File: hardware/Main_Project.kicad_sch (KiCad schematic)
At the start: 53 parts, among them J1 A_Motor, J2 B_Motor, J3 Power_Outputs, U1 L7805, U2 L298N, U4 L298N

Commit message: Motor Board
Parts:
- removed C6, C8, C9: 4.7uF, Capacitor_THT:CP_Radial_D10.0mm_P5.00mm, symbol Device:C_Polarized_US
- removed C7: 100nF, Capacitor_THT:C_Disc_D8.0mm_W2.5mm_P5.00mm, symbol Device:C
- removed D13, D14, D15, D16, D17, D18, D19, D20: D, Diode_THT:D_A-405_P10.16mm_Horizontal, symbol Device:D
- removed J1: A_Motor, TerminalBlock:TerminalBlock_bornier-2_P5.08mm, symbol Connector:Conn_01x04_Pin
- removed J2: B_Motor, TerminalBlock:TerminalBlock_bornier-2_P5.08mm, symbol Connector:Conn_01x04_Pin
- removed R10, R5, R6, R9: 1k, Resistor_THT:R_Axial_DIN0207_L6.3mm_D2.5mm_P10.16mm_Horizontal, symbol Device:R
- removed R3, R4, R7, R8: 10k, Resistor_THT:R_Axial_DIN0207_L6.3mm_D2.5mm_P10.16mm_Horizontal, symbol Device:R
- removed U4: L298N, Package_TO_SOT_THT:TO-220-15_P2.54x2.54mm_StaggerOdd_Lead4.58mm_Vertical, symbol Driver_Motor:L298N
- added H10, H9: HeatsinkMounting, new_winterbloom:M3_Heatsink_Mounting, symbol Mechanical:MountingHole
- added H5, H6, H7, H8: MountingHole, MountingHole:MountingHole_3mm, symbol Mechanical:MountingHole
- added J1: Motors_R, TerminalBlock:TerminalBlock_bornier-2_P5.08mm, symbol Connector:Conn_01x02_Socket
- added J2: Motors_L, TerminalBlock:TerminalBlock_bornier-2_P5.08mm, symbol Connector:Conn_01x02_Socket
- added J4: Motor_Control, Connector_Molex:Molex_KK-396_5273-06A_1x06_P3.96mm_Vertical, symbol Connector:Conn_01x06_Pin
- added J5: Motor_Power, TerminalBlock:TerminalBlock_bornier-3_P5.08mm, symbol Connector:Conn_01x03_Pin
- C5: footprint Capacitor_THT:CP_Radial_D10.0mm_P5.00mm -> Capacitor_THT:CP_Radial_D8.0mm_P3.50mm
- U1: footprint Package_TO_SOT_THT:TO-220-3_Vertical -> Package_TO_SOT_THT:TO-220-3_Horizontal_TabDown
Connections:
- net +12V: now also J5.1 (Pin_1)
- net +5V: now also J5.2 (Pin_2)
- net GND: now also U2.1 (SENSE_A), U2.15 (SENSE_B), J5.3 (Pin_3)
- net at D5.2 (A), D9.1 (K), U2.2 (OUT1): now also J2.1 (Pin_1)
- net at D10.1 (K), D6.2 (A), U2.3 (OUT2): now also J2.2 (Pin_2)
- net R_Enable: now reaches U2.11 (EnB)
- net R_Enable: now also J4.3 (Pin_3)
- net at D11.1 (K), D7.2 (A), U2.13 (OUT3): now also J1.1 (Pin_1)
- net at D12.1 (K), D8.2 (A), U2.14 (OUT4): now also J1.2 (Pin_2)
- net L_Enable: now reaches U2.6 (EnA)
- net L_Enable: now also J4.6 (Pin_6)
- net A_Motor1 renamed L_1
- net L_1: now also J4.1 (Pin_1)
- net A_Motor2 renamed L_2
- net L_2: now also J4.2 (Pin_2)
- net A_Motor3 renamed R_1
- net R_1: now also J4.5 (Pin_5)
- net A_Motor4 renamed R_2
- net R_2: now also J4.4 (Pin_4)
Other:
- note added: "Motor Driver"
- note removed: "Motor Driver A"
- note removed: "Motor Driver B"

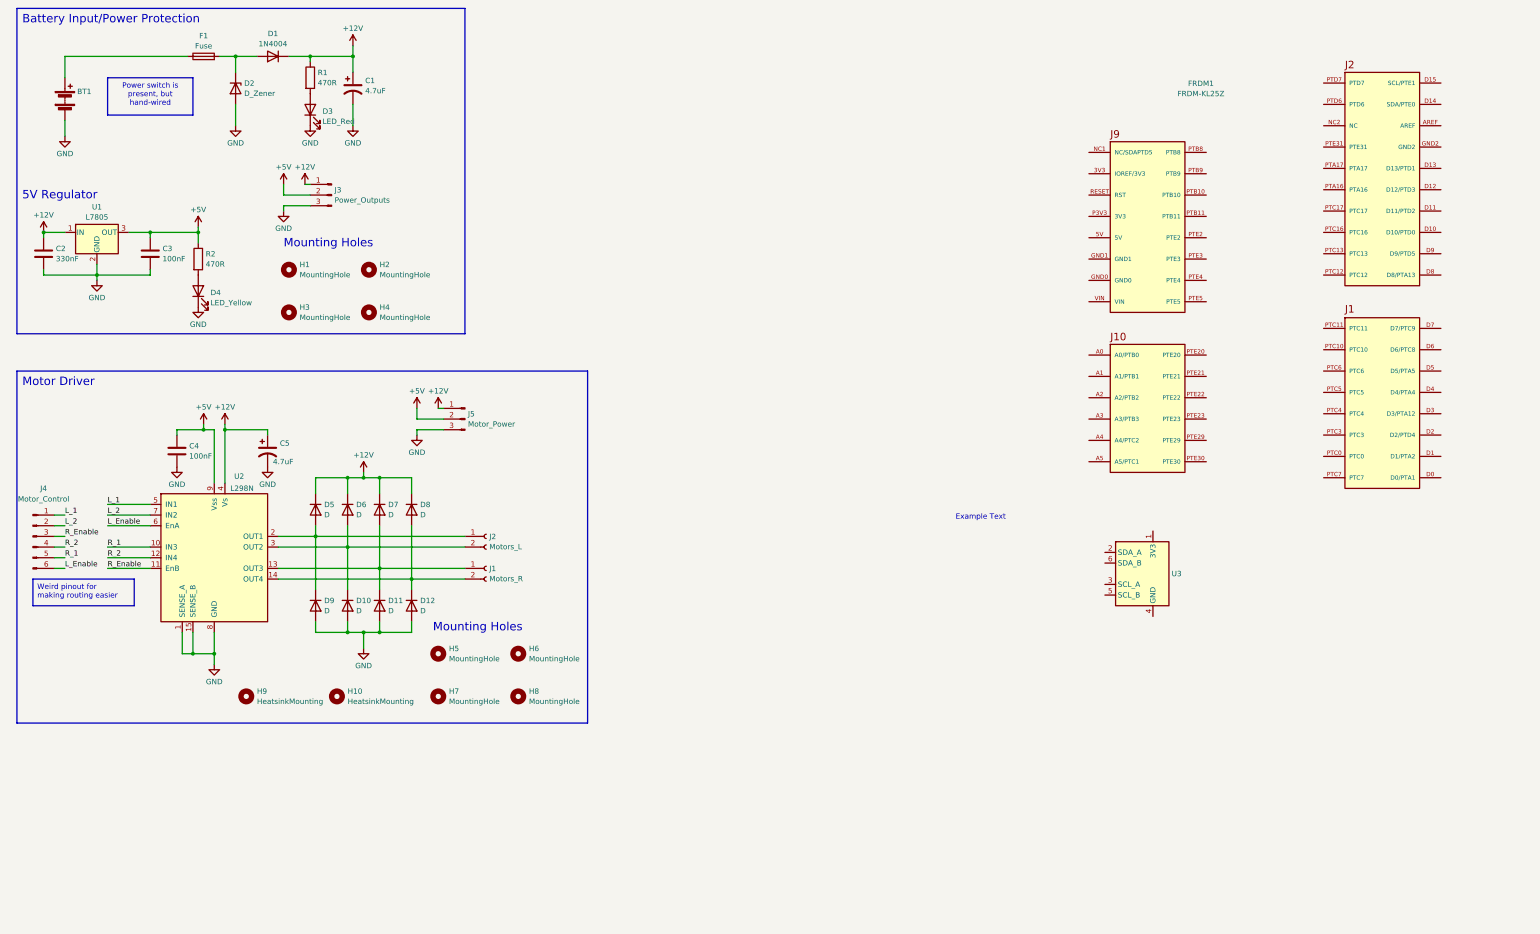
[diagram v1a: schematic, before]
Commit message: Colour Sensor board added and adjusted
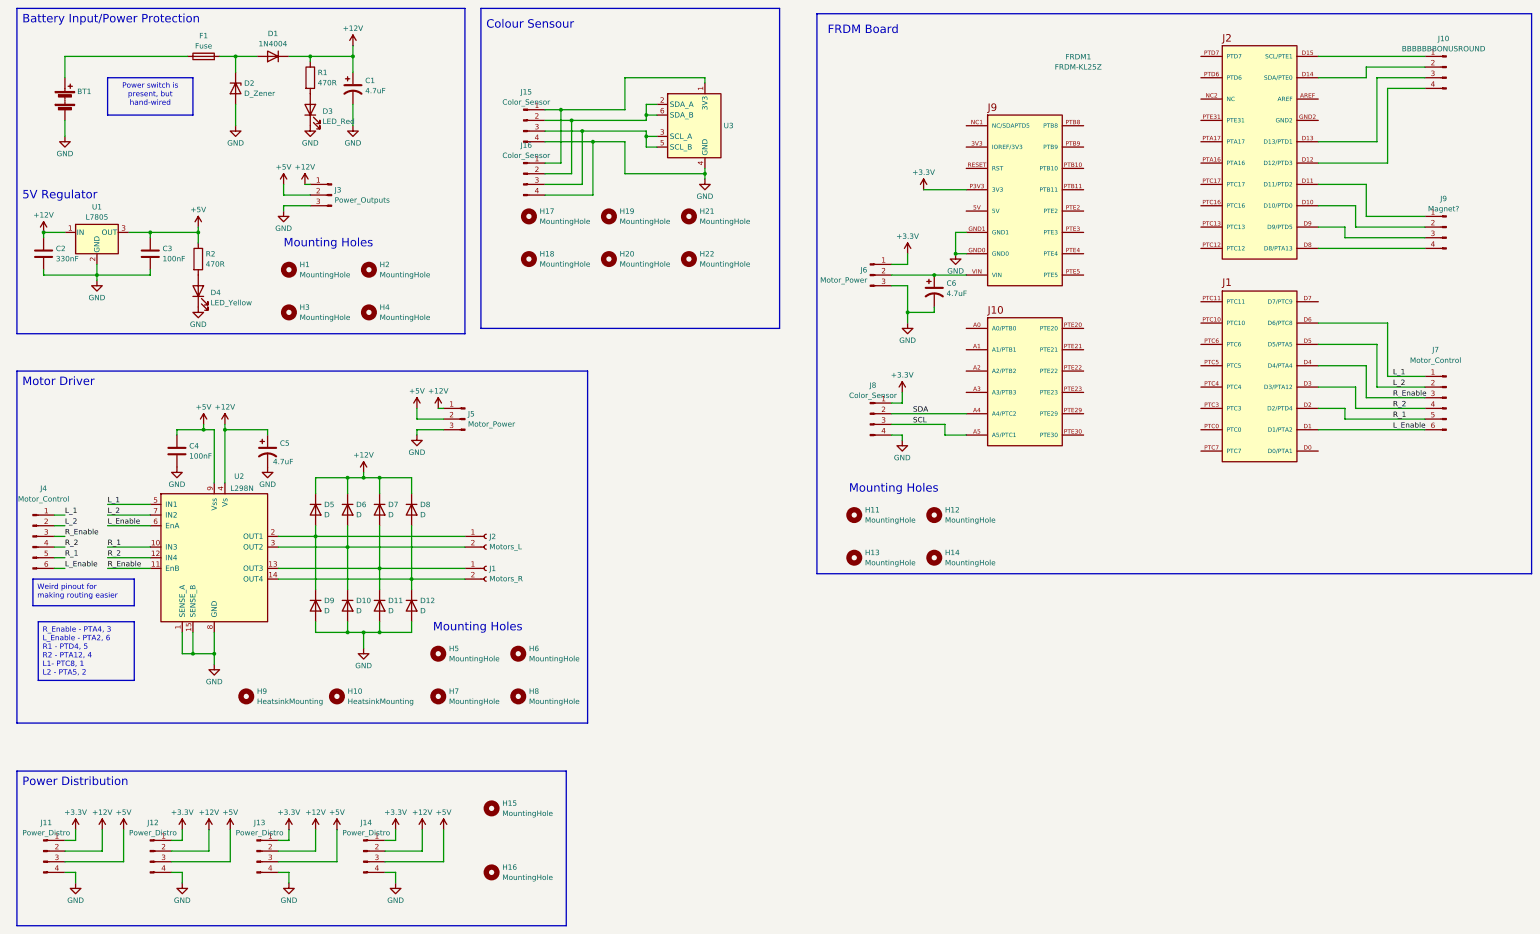
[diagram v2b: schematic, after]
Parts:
- added C6: 4.7uF, Capacitor_THT:CP_Radial_D8.0mm_P3.50mm, symbol Device:C_Polarized_US
- added H11, H12, H13, H14, H15, H16, H17, H18, H19, H20: MountingHole, MountingHole:MountingHole_3mm, symbol Mechanical:MountingHole
- added H21, H22: MountingHole, MountingHole:MountingHole_5.3mm_M5, symbol Mechanical:MountingHole
- added J10: BBBBBBBONUSROUND, Connector_Molex:Molex_KK-254_AE-6410-04A_1x04_P2.54mm_Vertical, symbol Connector:Conn_01x04_Pin
- added J11, J12, J13, J14: Power_Distro, TerminalBlock:TerminalBlock_bornier-4_P5.08mm, symbol Connector:Conn_01x04_Pin
- added J15, J16, J8: Color_Sensor, Connector_Molex:Molex_KK-254_AE-6410-04A_1x04_P2.54mm_Vertical, symbol Connector:Conn_01x04_Pin
- added J6: Motor_Power, TerminalBlock:TerminalBlock_bornier-3_P5.08mm, symbol Connector:Conn_01x03_Pin
- added J7: Motor_Control, Connector_Molex:Molex_KK-254_AE-6410-06A_1x06_P2.54mm_Vertical, symbol Connector:Conn_01x06_Pin
- added J9: Magnet?, Connector_Molex:Molex_KK-254_AE-6410-04A_1x04_P2.54mm_Vertical, symbol Connector:Conn_01x04_Pin
- J4: footprint Connector_Molex:Molex_KK-396_5273-06A_1x06_P3.96mm_Vertical -> Connector_Molex:Molex_KK-254_AE-6410-06A_1x06_P2.54mm_Vertical
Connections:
- net +12V: now also J11.2 (Pin_2), J12.2 (Pin_2), J13.2 (Pin_2), J14.2 (Pin_2)
- net +5V: now also J11.3 (Pin_3), J12.3 (Pin_3), J13.3 (Pin_3), J14.3 (Pin_3)
- net GND: now also FRDM1.GND0, FRDM1.GND1, U3.4 (GND), C6.2, J11.4 (Pin_4), J12.4 (Pin_4), J13.4 (Pin_4), J14.4 (Pin_4), J15.4 (Pin_4), J16.4 (Pin_4), J6.3 (Pin_3), J8.4 (Pin_4)
- net L_1: now also FRDM1.D6 (D6/PTC8), J7.1 (Pin_1)
- net L_2: now also FRDM1.D5 (D5/PTA5), J7.2 (Pin_2)
- net L_Enable: now also FRDM1.D1 (D1/PTA2), J7.6 (Pin_6)
- net R_1: now also FRDM1.D2 (D2/PTD4), J7.5 (Pin_5)
- net R_2: now also FRDM1.D3 (D3/PTA12), J7.4 (Pin_4)
- net R_Enable: now also FRDM1.D4 (D4/PTA4), J7.3 (Pin_3)
- net at U3.1 (3V3): now also J15.1 (Pin_1), J16.1 (Pin_1)
- net at U3.2 (SDA_A): now also U3.6 (SDA_B), J15.2 (Pin_2), J16.2 (Pin_2)
- net at U3.3 (SCL_A): now also U3.5 (SCL_B), J15.3 (Pin_3), J16.3 (Pin_3)
- net SDA: now reaches FRDM1.A4 (A4/PTC2)
- net SDA: now also J8.2 (Pin_2)
- net SCL: now reaches FRDM1.A5 (A5/PTC1)
- net SCL: now also J8.3 (Pin_3)
- net at FRDM1.D10 (D10/PTD0): now also J9.2 (Pin_2)
- net at FRDM1.D11 (D11/PTD2): now also J9.1 (Pin_1)
- net at FRDM1.D12 (D12/PTD3): now also J10.4 (Pin_4)
- net at FRDM1.D13 (D13/PTD1): now also J10.3 (Pin_3)
- net at FRDM1.D14 (SDA/PTE0): now also J10.2 (Pin_2)
- net at FRDM1.D15 (SCL/PTE1): now also J10.1 (Pin_1)
- net at FRDM1.D8 (D8/PTA13): now also J9.4 (Pin_4)
- net at FRDM1.D9 (D9/PTD5): now also J9.3 (Pin_3)
- net +3V3: now reaches FRDM1.P3V3 (3V3)
- net +3V3: now also J11.1 (Pin_1), J12.1 (Pin_1), J13.1 (Pin_1), J14.1 (Pin_1), J6.1 (Pin_1), J8.1 (Pin_1)
- net at FRDM1.VIN: now also C6.1, J6.2 (Pin_2)
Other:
- note added: "Colour Sensour"
- note added: "FRDM Board"
- note added: "Power Distribution"
- note removed: "Example Text"
- moved on the sheet: FRDM1, U3

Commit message: added notes for priority of tasks
xxx
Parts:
- added H23, H24: HeatsinkMounting, new_winterbloom:M3_Heatsink_Mounting, symbol Mechanical:MountingHole
- added H25, H26, H27, H28: MountingHole, MountingHole:MountingHole_3mm, symbol Mechanical:MountingHole
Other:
- note added: "Magnet Board"
- note added: "heatsink around MOS - should be same footprint as motor driver heatsink. diode: 1N4007"
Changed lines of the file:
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@@
+    (fill (type none))
+  )
+  (rectangle (start 289.306 165.608) (end 380.492 241.808)
+    (stroke (width 0) (type default))
     (fill (type none))
   )
@@
     (effects (font (size 2 2)) (justify left bottom))
   )
+  (text "heatsink around MOS - should be same footprint as motor driver heatsink.\ndiode: 1N4007"
+    (at 292.862 236.474 0)
+    (effects (font (size 1.27 1.27)) (justify left bottom))
+  )
   (text "5V Regulator" (at 20.32 71.12 0)
     (effects (font (size 2 2)) (justify left bottom))
@@
     (effects (font (size 2 2)) (justify left bottom))
   )
+  (text "Magnet Board" (at 292.608 172.212 0)
+    (effects (font (size 2 2)) (justify left bottom))
+  )
   (text "Motor Driver" (at 20.32 115.57 0)
     (effects (font (size 2 2)) (justify left bottom))
@@
         (path "/49595465-104c-4a4c-848b-e24eebb1e8d2"
           (reference "J12") (unit 1)
+        )
+      )
+    )
+  )
+  (symbol (lib_id "Mechanical:MountingHole") (at 361.95 169.926 0) (unit 1)
+    (in_bom yes) (on_board yes) (dnp no) (fields_autoplaced)
+    (property "Reference" "H27" (at 364.49 168.7139 0)
+      (effects (font (size 1.27 1.27)) (justify left))
+    )
+    (property "Value" "MountingHole" (at 364.49 171.1381 0)
+      (effects (font (size 1.27 1.27)) (justify left))
+    )
+    (property "Footprint" "MountingHole:MountingHole_3mm" (at 361.95 169.926 0)
+      (effects (font (size 1.27 1.27)) hide)
+    )
+    (property "Datasheet" "~" (at 361.95 169.926 0)
+      (effects (font (size 1.27 1.27)) hide)
+    )
+    (instances
+      (project "Main_Project"
+        (path "/49595465-104c-4a4c-848b-e24eebb1e8d2"
+          (reference "H27") (unit 1)
         )
       )
@@
         (path "/49595465-104c-4a4c-848b-e24eebb1e8d2"
           (reference "#PWR015") (unit 1)
+        )
+      )
+    )
+  )
+  (symbol (lib_id "Mechanical:MountingHole") (at 295.148 178.562 0) (unit 1)
+    (in_bom yes) (on_board yes) (dnp no) (fields_autoplaced)
+    (property "Reference" "H23" (at 297.688 177.3499 0)
+      (effects (font (size 1.27 1.27)) (justify left))
+    )
+    (property "Value" "HeatsinkMounting" (at 297.688 179.7741 0)
+      (effects (font (size 1.27 1.27)) (justify left))
+    )
+    (property "Footprint" "new_winterbloom:M3_Heatsink_Mounting" (at 295.148 178.562 0)
+      (effects (font (size 1.27 1.27)) hide)
+    )
+    (property "Datasheet" "~" (at 295.148 178.562 0)
+      (effects (font (size 1.27 1.27)) hide)
+    )
+    (instances
+      (project "Main_Project"
+        (path "/49595465-104c-4a4c-848b-e24eebb1e8d2"
+          (reference "H23") (unit 1)
         )
       )
@@
     )
   )
+  (symbol (lib_id "Mechanical:MountingHole") (at 361.95 180.086 0) (unit 1)
+    (in_bom yes) (on_board yes) (dnp no) (fields_autoplaced)
+    (property "Reference" "H28" (at 364.49 178.8739 0)
+      (effects (font (size 1.27 1.27)) (justify left))
+    )
+    (property "Value" "MountingHole" (at 364.49 181.2981 0)
+      (effects (font (size 1.27 1.27)) (justify left))
+    )
+    (property "Footprint" "MountingHole:MountingHole_3mm" (at 361.95 180.086 0)
+      (effects (font (size 1.27 1.27)) hide)
+    )
+    (property "Datasheet" "~" (at 361.95 180.086 0)
+      (effects (font (size 1.27 1.27)) hide)
+    )
+    (instances
+      (project "Main_Project"
+        (path "/49595465-104c-4a4c-848b-e24eebb1e8d2"
+          (reference "H28") (unit 1)
+        )
+      )
+    )
+  )
   (symbol (lib_id "PCM_4ms_Power-symbol:+12V") (at 101.6 135.89 0) (unit 1)
     (in_bom yes) (on_board yes) (dnp no) (fields_autoplaced)
@@
         (path "/49595465-104c-4a4c-848b-e24eebb1e8d2"
           (reference "#PWR021") (unit 1)
+        )
+      )
+    )
+  )
+  (symbol (lib_id "Mechanical:MountingHole") (at 342.9 169.926 0) (unit 1)
+    (in_bom yes) (on_board yes) (dnp no) (fields_autoplaced)
+    (property "Reference" "H25" (at 345.44 168.7139 0)
+      (effects (font (size 1.27 1.27)) (justify left))
+    )
+    (property "Value" "MountingHole" (at 345.44 171.1381 0)
+      (effects (font (size 1.27 1.27)) (justify left))
+    )
+    (property "Footprint" "MountingHole:MountingHole_3mm" (at 342.9 169.926 0)
+      (effects (font (size 1.27 1.27)) hide)
+    )
+    (property "Datasheet" "~" (at 342.9 169.926 0)
+      (effects (font (size 1.27 1.27)) hide)
+    )
+    (instances
+      (project "Main_Project"
+        (path "/49595465-104c-4a4c-848b-e24eebb1e8d2"
+          (reference "H25") (unit 1)
         )
       )
@@
         (path "/49595465-104c-4a4c-848b-e24eebb1e8d2"
           (reference "U1") (unit 1)
+        )
+      )
+    )
+  )
+  (symbol (lib_id "Mechanical:MountingHole") (at 316.738 178.562 0) (unit 1)
+    (in_bom yes) (on_board yes) (dnp no) (fields_autoplaced)
+    (property "Reference" "H24" (at 319.278 177.3499 0)
+      (effects (font (size 1.27 1.27)) (justify left))
+    )
+    (property "Value" "HeatsinkMounting" (at 319.278 179.7741 0)
+      (effects (font (size 1.27 1.27)) (justify left))
+    )
+    (property "Footprint" "new_winterbloom:M3_Heatsink_Mounting" (at 316.738 178.562 0)
+      (effects (font (size 1.27 1.27)) hide)
+    )
+    (property "Datasheet" "~" (at 316.738 178.562 0)
+      (effects (font (size 1.27 1.27)) hide)
+    )
+    (instances
+      (project "Main_Project"
+        (path "/49595465-104c-4a4c-848b-e24eebb1e8d2"
+          (reference "H24") (unit 1)
         )
       )
@@
         )
       )
+    )
+  )
+  (symbol (lib_id "Mechanical:MountingHole") (at 342.9 180.086 0) (unit 1)
+    (in_bom yes) (on_board yes) (dnp no) (fields_autoplaced)
+    (property "Reference" "H26" (at 345.44 178.8739 0)
+      (effects (font (size 1.27 1.27)) (justify left))
+    )
+    (property "Value" "MountingHole" (at 345.44 181.2981 0)
+      (effects (font (size 1.27 1.27)) (justify left))
+    )
+    (property "Footprint" "MountingHole:MountingHole_3mm" (at 342.9 180.086 0)
+      (effects (font (size 1.27 1.27)) hide)
+    )
+    (property "Datasheet" "~" (at 342.9 180.086 0)
+      (effects (font (size 1.27 1.27)) hide)
+    )
+    (instances
+      (project "Main_Project"
+        (path "/49595465-104c-4a4c-848b-e24eebb1e8d2"
+          (reference "H26") (unit 1)
+        )
+      )
